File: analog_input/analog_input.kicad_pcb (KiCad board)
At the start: 2 copper layers, 25.4 x 25.4 mm, 22 parts, among them J1 Port 1, J2 Port 2, J3 PPS IO, J4 Power Input, U1 C226S, U2 INA2181, U3 C226S

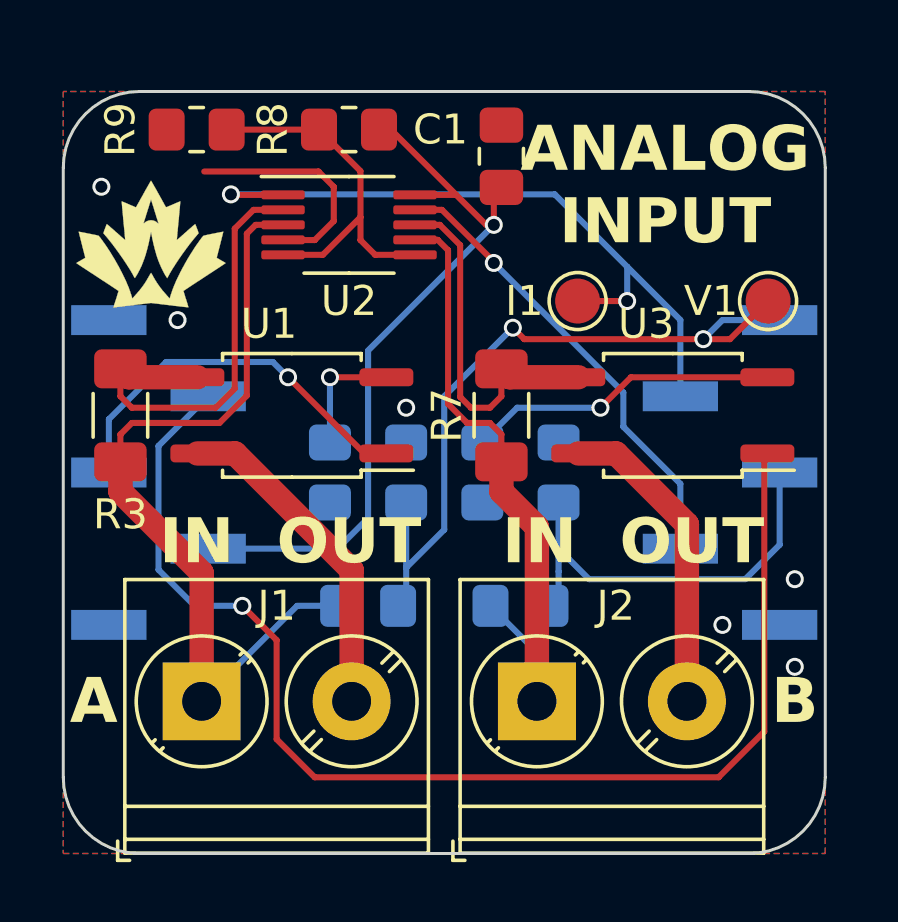
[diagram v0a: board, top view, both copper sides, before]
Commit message: Address review comments, finish routing HILT main board
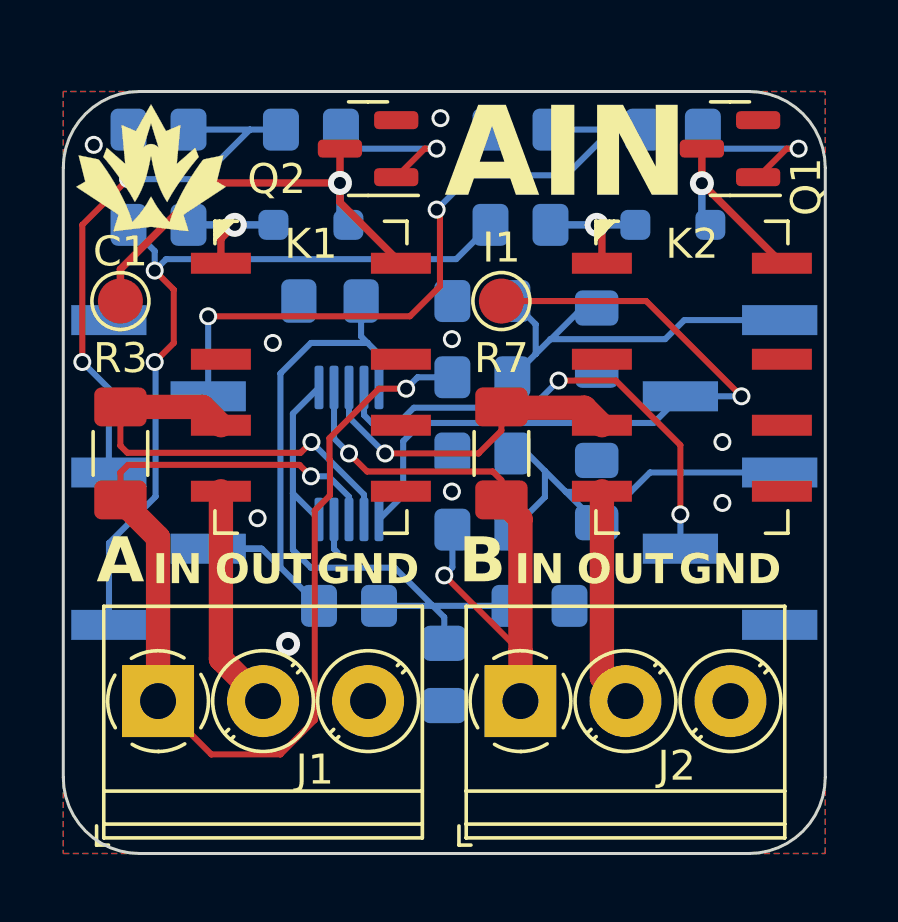
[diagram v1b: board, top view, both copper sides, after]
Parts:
- removed the G*** at (114.7, 88.9)
- removed the G*** at (124.5, 88.6)
- removed U1, U3: C226S, Package_SO:SO-4_4.4x3.9mm_P2.54mm
- added C2: 100n, Capacitor_SMD:C_0805_2012Metric_Pad1.18x1.45mm_HandSolder, B.Cu at (129.5, 92.1)
- added C3: 100n, Capacitor_SMD:C_0805_2012Metric_Pad1.18x1.45mm_HandSolder, B.Cu at (129.5, 97.2)
- added C4: 100n, Capacitor_SMD:C_0805_2012Metric_Pad1.18x1.45mm_HandSolder, B.Cu at (124.5, 103.3)
- added D1: 1N4148WX, Diode_SMD:D_SOD-323_HandSoldering, B.Cu at (132.1, 88.3)
- added D2: 1N4148WX, Diode_SMD:D_SOD-323_HandSoldering, B.Cu at (120.0, 88.3)
- added G***: LOGO, Team_Logo:Logo_SilkScreen_5mm, F.Cu at (114.7, 86.4)
- added G***: LOGO, Team_Logo:Logo_SilkScreen_5mm, B.Cu at (123.4, 106.8)
- added K1: IM02G, Relay_SMD:Relay_2P2T_10x6mm_TE_IMxxG, F.Cu at (120.0, 93.3)
- added K2: IM02G, Relay_SMD:Relay_2P2T_10x6mm_TE_IMxxG, F.Cu at (132.7, 93.3)
- added Q1: BC846B, Package_TO_SOT_SMD:SOT-23, F.Cu at (134.0, 85.7)
- added Q2: BC846B, Package_TO_SOT_SMD:SOT-23, F.Cu at (121.9, 85.7)
- added R11: 16R, Resistor_SMD:R_0805_2012Metric_Pad1.20x1.40mm_HandSolder, B.Cu at (114.9, 88.3)
- added R12: 10k, Resistor_SMD:R_0805_2012Metric_Pad1.20x1.40mm_HandSolder, B.Cu at (127.0, 85.1)
- added R13: 1k, Resistor_SMD:R_0805_2012Metric_Pad1.20x1.40mm_HandSolder, B.Cu at (132.1, 85.1)
- added R14: 16R, Resistor_SMD:R_0805_2012Metric_Pad1.20x1.40mm_HandSolder, B.Cu at (127.0, 88.3)
- C1, R8, R9: moved to B.Cu
- J1: value Port 1 -> Port A; footprint TerminalBlock_Phoenix:TerminalBlock_Phoenix_PT-1,5-2-5.0-H_1x02_P5.00mm_Horizontal -> TerminalBlock_Phoenix:TerminalBlock_Phoenix_PT-1,5-3-3.5-H_1x03_P3.50mm_Horizontal
- J2: value Port 2 -> Port B; footprint TerminalBlock_Phoenix:TerminalBlock_Phoenix_PT-1,5-2-5.0-H_1x02_P5.00mm_Horizontal -> TerminalBlock_Phoenix:TerminalBlock_Phoenix_PT-1,5-3-3.5-H_1x03_P3.50mm_Horizontal
- R1, R4: value 100k -> 100k 1%
- R10: value 383R -> 1k
- R3, R7: value 20mR -> 7.5mR
- R6: value 383R -> 10k
- TP1: value V1 -> C1
- U2: value INA2181 -> INA2181A3; moved to B.Cu
- moved TP1 21.6 mm to (113.7, 90.8)
- moved R9 19.6 mm to (127.6, 101.0), turned to 0 degrees
- moved R8 15.9 mm to (121.3, 101.0), turned to 180 degrees
- moved R10 12.8 mm to (120.0, 85.1), turned to 180 degrees
- moved R6 12.8 mm to (114.9, 85.1), turned to 0 degrees
- moved R1 8.52 mm to (125.7, 93.3)
- moved U2 7.62 mm to (121.3, 95.9), turned to 90 degrees
- moved C1 7.48 mm to (120.7, 90.8), turned to 180 degrees
- moved R2 6.25 mm to (125.7, 90.8), turned to 180 degrees
- moved R4 2.84 mm to (125.7, 98.4)
- moved R5 2.62 mm to (125.7, 95.9), turned to 180 degrees
- moved TP2 2.54 mm to (126.4, 90.8)
- moved J1 1.45 mm to (114.9, 104.1)
- moved R3 1.27 mm to (113.7, 95.9)
- moved R7 1.27 mm to (126.4, 95.9)
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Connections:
- R10 pad 1: /ON2_N -> Net-(Q2-B)
- R10 pad 2: GND -> /ON1
- R6 pad 1: /ON1_N -> GND
- R6 pad 2: GND -> /ON1
- TP1 pad 1: /VSENS1 -> /CTRL1
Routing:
- net +5V: track 0.00 -> 26.7 mm, vias 0 -> 2
- net /ON2: track 41.4 -> 23.4 mm, vias 1 -> 2
- net /CTRL1: track 0.00 -> 15.7 mm, vias 0 -> 1
- net /VSENS1: track 25.0 -> 13.8 mm, vias 2 -> 0
- net /IN1: track 27.4 -> 38.0 mm, vias 0 -> 2
- net /ON2_N: track 10.4 -> 0.00 mm, vias 1 -> 0
- net GND: track 7.63 -> 1.15 mm, vias 6 -> 9
- net /CTRL2: track 0.00 -> 6.43 mm, vias 0 -> 1
- net /VREF: track 12.5 -> 18.2 mm
- net /ON1: track 13.1 -> 18.6 mm, vias 1 -> 2
- net +3V3: track 24.6 -> 19.2 mm, vias 1 -> 0
- net Net-(Q2-B): track 0.00 -> 5.20 mm, vias 0 -> 1
- net Net-(Q1-B): track 0.00 -> 5.20 mm, vias 0 -> 1
- net Net-(D2-K): track 0.00 -> 4.30 mm, vias 0 -> 1
- net Net-(D1-K): track 0.00 -> 4.18 mm, vias 0 -> 1
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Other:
- board text added: "2023/ 05/02"
- board text added: "AIN"
- board text added: "Cutlass R1 Jack C"
- board text added: "GND"
- board text removed: "2023/ 04/15"
- board text removed: "ANALOG INPUT"
- board text removed: "Cutlass R1 Jack C."

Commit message: Address review comments
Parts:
- moved Q1 0.51 mm to (133.5, 85.7)
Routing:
- net /CTRL2: track 6.43 -> 7.10 mm
- net Net-(Q1-B): track 5.20 -> 4.69 mm
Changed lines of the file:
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@@
   )
   (footprint "Package_TO_SOT_SMD:SOT-23" (layer "F.Cu")
-    (at 133.985 85.725 180)
+    (at 133.477 85.725 180)
     (descr "SOT, 3 Pin (https://www.jedec.org/system/files/docs/to-236h.pdf variant AB), generated with kicad-footprint-generator ipc_gullwing_generator.py")
     (tags "SOT TO_SOT_SMD")
@@
     (effects (font (size 1 1) (thickness 0.15)) (justify left bottom mirror))
   )
-  (gr_text "AIN" (at 124.46 87.63) (layer "F.SilkS")
+  (gr_text "AIN" (at 123.952 87.63) (layer "F.SilkS")
     (effects (font (size 3 3) (thickness 0.6) bold) (justify left bottom))
   )
@@
   (segment (start 117.015 97.145) (end 117.015 102.735) (width 0.8128) (layer "F.Cu") (net 5))
   (via (at 118.745 92.202) (size 0.6) (drill 0.4) (layers "F.Cu" "B.Cu") (free) (net 6))
-  (via (at 119.253 102.235) (size 0.8) (drill 0.4) (layers "F.Cu" "B.Cu") (free) (net 6))
+  (via (at 119.253 102.235) (size 0.6) (drill 0.4) (layers "F.Cu" "B.Cu") (free) (net 6))
   (via (at 124.714 92.075) (size 0.6) (drill 0.4) (layers "F.Cu" "B.Cu") (free) (net 6))
   (via (at 124.714 97.155) (size 0.6) (drill 0.4) (layers "F.Cu" "B.Cu") (free) (net 6))
@@
   (segment (start 129.54 88.265) (end 129.715 88.44) (width 0.25) (layer "F.Cu") (net 14))
   (segment (start 129.715 88.44) (end 129.715 89.545) (width 0.25) (layer "F.Cu") (net 14))
-  (via (at 129.54 88.265) (size 0.8) (drill 0.4) (layers "F.Cu" "B.Cu") (net 14))
+  (via (at 129.54 88.265) (size 0.6) (drill 0.4) (layers "F.Cu" "B.Cu") (net 14))
   (segment (start 129.54 88.265) (end 128 88.265) (width 0.25) (layer "B.Cu") (net 14))
   (segment (start 129.54 88.265) (end 130.83 88.265) (width 0.25) (layer "B.Cu") (net 14))
@@
   (segment (start 117.015 88.725) (end 117.015 89.545) (width 0.25) (layer "F.Cu") (net 19))
   (segment (start 117.475 88.265) (end 117.015 88.725) (width 0.25) (layer "F.Cu") (net 19))
-  (via (at 117.475 88.265) (size 0.8) (drill 0.4) (layers "F.Cu" "B.Cu") (net 19))
+  (via (at 117.475 88.265) (size 0.6) (drill 0.4) (layers "F.Cu" "B.Cu") (net 19))
   (segment (start 117.475 88.265) (end 118.765 88.265) (width 0.25) (layer "B.Cu") (net 19))
   (segment (start 117.475 88.265) (end 115.935 88.265) (width 0.25) (layer "B.Cu") (net 19))
-  (segment (start 135.8725 85.725) (end 134.9225 86.675) (width 0.2032) (layer "F.Cu") (net 21))
-  (segment (start 136.271 85.725) (end 135.8725 85.725) (width 0.2032) (layer "F.Cu") (net 21))
-  (via (at 136.271 85.725) (size 0.6) (drill 0.4) (layers "F.Cu" "B.Cu") (net 21))
-  (segment (start 136.271 85.725) (end 133.715 85.725) (width 0.2032) (layer "B.Cu") (net 21))
+  (segment (start 135.3645 85.725) (end 134.4145 86.675) (width 0.2032) (layer "F.Cu") (net 21))
+  (segment (start 135.763 85.725) (end 135.3645 85.725) (width 0.2032) (layer "F.Cu") (net 21))
+  (via (at 135.763 85.725) (size 0.6) (drill 0.4) (layers "F.Cu" "B.Cu") (net 21))
   (segment (start 133.715 85.725) (end 133.08 85.09) (width 0.2032) (layer "B.Cu") (net 21))
+  (segment (start 135.763 85.725) (end 133.715 85.725) (width 0.2032) (layer "B.Cu") (net 21))
   (segment (start 123.8075 85.725) (end 122.8575 86.675) (width 0.2032) (layer "F.Cu") (net 23))
   (segment (start 124.206 85.725) (end 123.8075 85.725) (width 0.2032) (layer "F.Cu") (net 23))
@@
   (segment (start 121.65 85.725) (end 121.015 85.09) (width 0.2032) (layer "B.Cu") (net 23))
   (segment (start 124.206 85.725) (end 121.65 85.725) (width 0.2032) (layer "B.Cu") (net 23))
-  (segment (start 133.0475 86.8775) (end 133.0475 85.725) (width 0.25) (layer "F.Cu") (net 29))
-  (segment (start 133.0475 86.8775) (end 135.715 89.545) (width 0.25) (layer "F.Cu") (net 29))
-  (via (at 133.0475 86.8775) (size 0.8) (drill 0.4) (layers "F.Cu" "B.Cu") (net 29))
-  (segment (start 133.0475 87.9825) (end 133.33 88.265) (width 0.25) (layer "B.Cu") (net 29))
-  (segment (start 133.0475 86.8775) (end 133.0475 87.9825) (width 0.25) (layer "B.Cu") (net 29))
+  (segment (start 132.588 86.868) (end 132.5395 86.8195) (width 0.25) (layer "F.Cu") (net 29))
+  (segment (start 132.5395 86.8195) (end 132.5395 85.725) (width 0.25) (layer "F.Cu") (net 29))
+  (segment (start 133.038 86.868) (end 135.715 89.545) (width 0.25) (layer "F.Cu") (net 29))
+  (segment (start 132.588 86.868) (end 133.038 86.868) (width 0.25) (layer "F.Cu") (net 29))
+  (via (at 132.588 86.868) (size 0.6) (drill 0.4) (layers "F.Cu" "B.Cu") (net 29))
+  (segment (start 132.588 87.523) (end 133.33 88.265) (width 0.25) (layer "B.Cu") (net 29))
+  (segment (start 132.588 86.868) (end 132.588 87.523) (width 0.25) (layer "B.Cu") (net 29))
   (segment (start 120.9825 86.868) (end 120.9825 87.5125) (width 0.25) (layer "F.Cu") (net 30))
   (segment (start 120.9825 86.868) (end 120.9825 85.725) (width 0.25) (layer "F.Cu") (net 30))
@@
   (segment (start 120.9825 87.5125) (end 123.015 89.545) (width 0.25) (layer "F.Cu") (net 30))
   (segment (start 116.54134 86.868) (end 113.665 89.74434) (width 0.25) (layer "F.Cu") (net 30))
-  (via (at 120.9825 86.868) (size 0.8) (drill 0.4) (layers "F.Cu" "B.Cu") (net 30))
+  (via (at 120.9825 86.868) (size 0.6) (drill 0.4) (layers "F.Cu" "B.Cu") (net 30))
   (segment (start 120.9825 86.868) (end 120.9825 87.9825) (width 0.25) (layer "B.Cu") (net 30))
   (segment (start 120.9825 87.9825) (end 121.265 88.265) (width 0.25) (layer "B.Cu") (net 30))
